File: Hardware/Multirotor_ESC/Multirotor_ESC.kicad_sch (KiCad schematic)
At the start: 0 parts

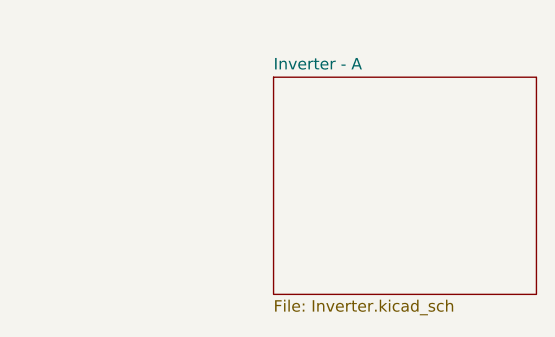
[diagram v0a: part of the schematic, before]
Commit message: Added Phase Half-Bridge Circuit
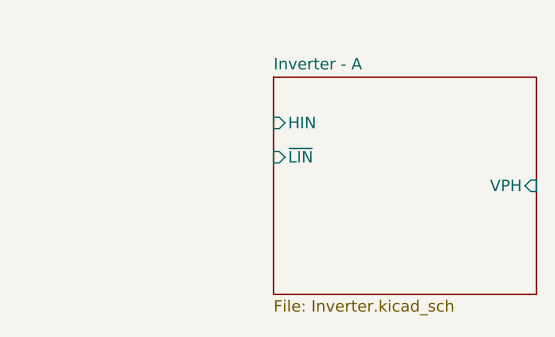
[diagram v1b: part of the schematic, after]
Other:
- sheet Inverter - A ports: added HIN, VPH, ~{LIN}; removed none
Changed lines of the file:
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@@
       (effects (font (size 1.27 1.27)) (justify left top))
+    )
+    (pin "HIN" input (at 135.89 74.93 180)
+      (effects (font (size 1.27 1.27)) (justify left))
+    )
+    (pin "~{LIN}" input (at 135.89 78.74 180)
+      (effects (font (size 1.27 1.27)) (justify left))
+    )
+    (pin "VPH" input (at 165.1 81.915 0)
+      (effects (font (size 1.27 1.27)) (justify right))
     )
   )
@@
       (reference "#PWR?") (unit 1) (value "+BATT") (footprint "")
     )
+    (path "/97e0d8f2-3fb5-4132-bc5b-5e7a03ef2bdb/1fb1d06b-db4f-42d1-9251-2385d7bb41cf"
+      (reference "#PWR?") (unit 1) (value "GND") (footprint "")
+    )
+    (path "/97e0d8f2-3fb5-4132-bc5b-5e7a03ef2bdb/268e3d62-216c-4de0-ba8e-c1e5772f9b92"
+      (reference "#PWR?") (unit 1) (value "+BATT") (footprint "")
+    )
+    (path "/97e0d8f2-3fb5-4132-bc5b-5e7a03ef2bdb/3ca54db6-939c-4fbf-b276-1cff5ae9ba60"
+      (reference "#PWR?") (unit 1) (value "GND") (footprint "")
+    )
+    (path "/97e0d8f2-3fb5-4132-bc5b-5e7a03ef2bdb/574bb345-e256-4887-850f-b8dd578552c6"
+      (reference "#PWR?") (unit 1) (value "GND") (footprint "")
+    )
     (path "/6925d0aa-6a6d-48e8-beb5-c68f11da7a23/727fd17b-2514-45b6-a580-bec774717ec9"
       (reference "#PWR?") (unit 1) (value "GND") (footprint "")
@@
       (reference "#PWR?") (unit 1) (value "+3V3") (footprint "")
     )
+    (path "/97e0d8f2-3fb5-4132-bc5b-5e7a03ef2bdb/85d6321a-5bef-4003-9692-bf4bf59b33cc"
+      (reference "#PWR?") (unit 1) (value "GND") (footprint "")
+    )
+    (path "/97e0d8f2-3fb5-4132-bc5b-5e7a03ef2bdb/9fbafe7a-b33b-4a4e-b582-f71e3fabfd8e"
+      (reference "#PWR?") (unit 1) (value "+3V3") (footprint "")
+    )
+    (path "/97e0d8f2-3fb5-4132-bc5b-5e7a03ef2bdb/a8699dfc-87f8-4653-a4c7-dfff237c52ef"
+      (reference "#PWR?") (unit 1) (value "GND") (footprint "")
+    )
+    (path "/97e0d8f2-3fb5-4132-bc5b-5e7a03ef2bdb/f2234975-42e9-48d9-8b53-ca208cf03c75"
+      (reference "#PWR?") (unit 1) (value "+BATT") (footprint "")
+    )
+    (path "/97e0d8f2-3fb5-4132-bc5b-5e7a03ef2bdb/089f6096-ba98-4aaa-8bdf-ede1c7ae272e"
+      (reference "C?") (unit 1) (value "47μF") (footprint "")
+    )
     (path "/6925d0aa-6a6d-48e8-beb5-c68f11da7a23/666b110b-64b3-4b1b-b648-8cefb6eb0bcb"
       (reference "C?") (unit 1) (value "100nF") (footprint "")
@@
     )
     (path "/6925d0aa-6a6d-48e8-beb5-c68f11da7a23/7d444e59-e85f-4b36-a7ee-89b1c2dc2bc1"
-      (reference "C?") (unit 1) (value "47uF") (footprint "")
+      (reference "C?") (unit 1) (value "47μF") (footprint "")
     )
     (path "/6925d0aa-6a6d-48e8-beb5-c68f11da7a23/7f018784-9df3-41a8-a771-7183d616fcb0"
       (reference "C?") (unit 1) (value "100nF") (footprint "")
+    )
+    (path "/97e0d8f2-3fb5-4132-bc5b-5e7a03ef2bdb/bd46a2b4-b92a-4936-9d7c-11eee0e384a6"
+      (reference "C?") (unit 1) (value "1μF") (footprint "")
+    )
+    (path "/97e0d8f2-3fb5-4132-bc5b-5e7a03ef2bdb/bd887885-43f0-4985-a387-d5bffe1a774c"
+      (reference "C?") (unit 1) (value "1μF") (footprint "")
+    )
+    (path "/97e0d8f2-3fb5-4132-bc5b-5e7a03ef2bdb/c9a91d26-ba86-4e5a-a536-67083e503fde"
+      (reference "C?") (unit 1) (value "1nF") (footprint "")
+    )
+    (path "/97e0d8f2-3fb5-4132-bc5b-5e7a03ef2bdb/cd75599b-50b9-4b16-8dec-26d684651b26"
+      (reference "C?") (unit 1) (value "100nF") (footprint "")
+    )
+    (path "/97e0d8f2-3fb5-4132-bc5b-5e7a03ef2bdb/d7576022-7064-48aa-bc88-f7217e8093a0"
+      (reference "C?") (unit 1) (value "10nF") (footprint "")
     )
     (path "/6925d0aa-6a6d-48e8-beb5-c68f11da7a23/e44df006-a55a-47e0-86b1-17debb1f8182"
@@
       (reference "D?") (unit 1) (value "LED") (footprint "")
     )
+    (path "/97e0d8f2-3fb5-4132-bc5b-5e7a03ef2bdb/2902243c-a616-4e0b-b976-e66ba39b0725"
+      (reference "D?") (unit 1) (value "D_TVS") (footprint "")
+    )
+    (path "/97e0d8f2-3fb5-4132-bc5b-5e7a03ef2bdb/ae845764-3102-4eea-9c30-798c6cae01d9"
+      (reference "D?") (unit 1) (value "D_Schottky") (footprint "")
+    )
     (path "/6925d0aa-6a6d-48e8-beb5-c68f11da7a23/af026ffe-ca2f-412b-8e63-3ecf96ad32af"
       (reference "D?") (unit 1) (value "D_TVS") (footprint "")
@@
       (reference "L?") (unit 1) (value "120R") (footprint "")
     )
+    (path "/97e0d8f2-3fb5-4132-bc5b-5e7a03ef2bdb/48372f14-952c-4ead-9841-6a6b01cb6ba9"
+      (reference "Q?") (unit 1) (value "SIR182DP-T1-RE3") (footprint "")
+    )
+    (path "/97e0d8f2-3fb5-4132-bc5b-5e7a03ef2bdb/9247a4d0-19a2-4ebd-8ef1-fdbc5bc16073"
+      (reference "Q?") (unit 1) (value "SIR182DP-T1-RE3") (footprint "")
+    )
+    (path "/97e0d8f2-3fb5-4132-bc5b-5e7a03ef2bdb/13ac03c9-514f-4610-a1ef-8c14da688496"
+      (reference "R?") (unit 1) (value "4.7kΩ") (footprint "")
+    )
     (path "/6925d0aa-6a6d-48e8-beb5-c68f11da7a23/248ead7f-752e-40c0-bb8c-4be19db10e0d"
       (reference "R?") (unit 1) (value "75kΩ") (footprint "")
+    )
+    (path "/97e0d8f2-3fb5-4132-bc5b-5e7a03ef2bdb/2623340c-6824-413a-b561-66c38b004f8f"
+      (reference "R?") (unit 1) (value "100Ω") (footprint "")
     )
     (path "/6925d0aa-6a6d-48e8-beb5-c68f11da7a23/30884663-b4d1-4804-b0f3-0861de72726b"
@@
       (reference "R?") (unit 1) (value "110kΩ") (footprint "")
     )
+    (path "/97e0d8f2-3fb5-4132-bc5b-5e7a03ef2bdb/5b0936e7-7161-47fa-9186-e44375fa52b6"
+      (reference "R?") (unit 1) (value "100Ω") (footprint "")
+    )
+    (path "/97e0d8f2-3fb5-4132-bc5b-5e7a03ef2bdb/5e26f97d-fab6-49a2-a541-bc2264f9522b"
+      (reference "R?") (unit 1) (value "2mΩ") (footprint "")
+    )
     (path "/6925d0aa-6a6d-48e8-beb5-c68f11da7a23/690f7831-bbd0-434d-9bf7-2f33f2b678b2"
       (reference "R?") (unit 1) (value "12kΩ") (footprint "")
@@
       (reference "R?") (unit 1) (value "1kΩ") (footprint "")
     )
+    (path "/97e0d8f2-3fb5-4132-bc5b-5e7a03ef2bdb/aca084b7-8df0-4d93-9d6c-b5b0ceddd281"
+      (reference "R?") (unit 1) (value "1kΩ") (footprint "")
+    )
     (path "/6925d0aa-6a6d-48e8-beb5-c68f11da7a23/dbf9d707-36a7-44c9-8154-2c0ba309d498"
       (reference "R?") (unit 1) (value "24kΩ") (footprint "")
+    )
+    (path "/97e0d8f2-3fb5-4132-bc5b-5e7a03ef2bdb/e00eda02-ebfb-4c4b-9080-81449d9715cf"
+      (reference "R?") (unit 1) (value "1kΩ") (footprint "")
     )
     (path "/6925d0aa-6a6d-48e8-beb5-c68f11da7a23/fe9632fd-6344-4254-bb7c-69d57a7190da"
       (reference "R?") (unit 1) (value "4.7kΩ") (footprint "")
     )
+    (path "/97e0d8f2-3fb5-4132-bc5b-5e7a03ef2bdb/6d254fa2-e95b-4d81-85ec-158eceec45b3"
+      (reference "U?") (unit 1) (value "INA180") (footprint "Package_TO_SOT_SMD:SOT-23-5")
+    )
     (path "/6925d0aa-6a6d-48e8-beb5-c68f11da7a23/c13cf85f-c98f-45ba-8820-17fab98a6470"

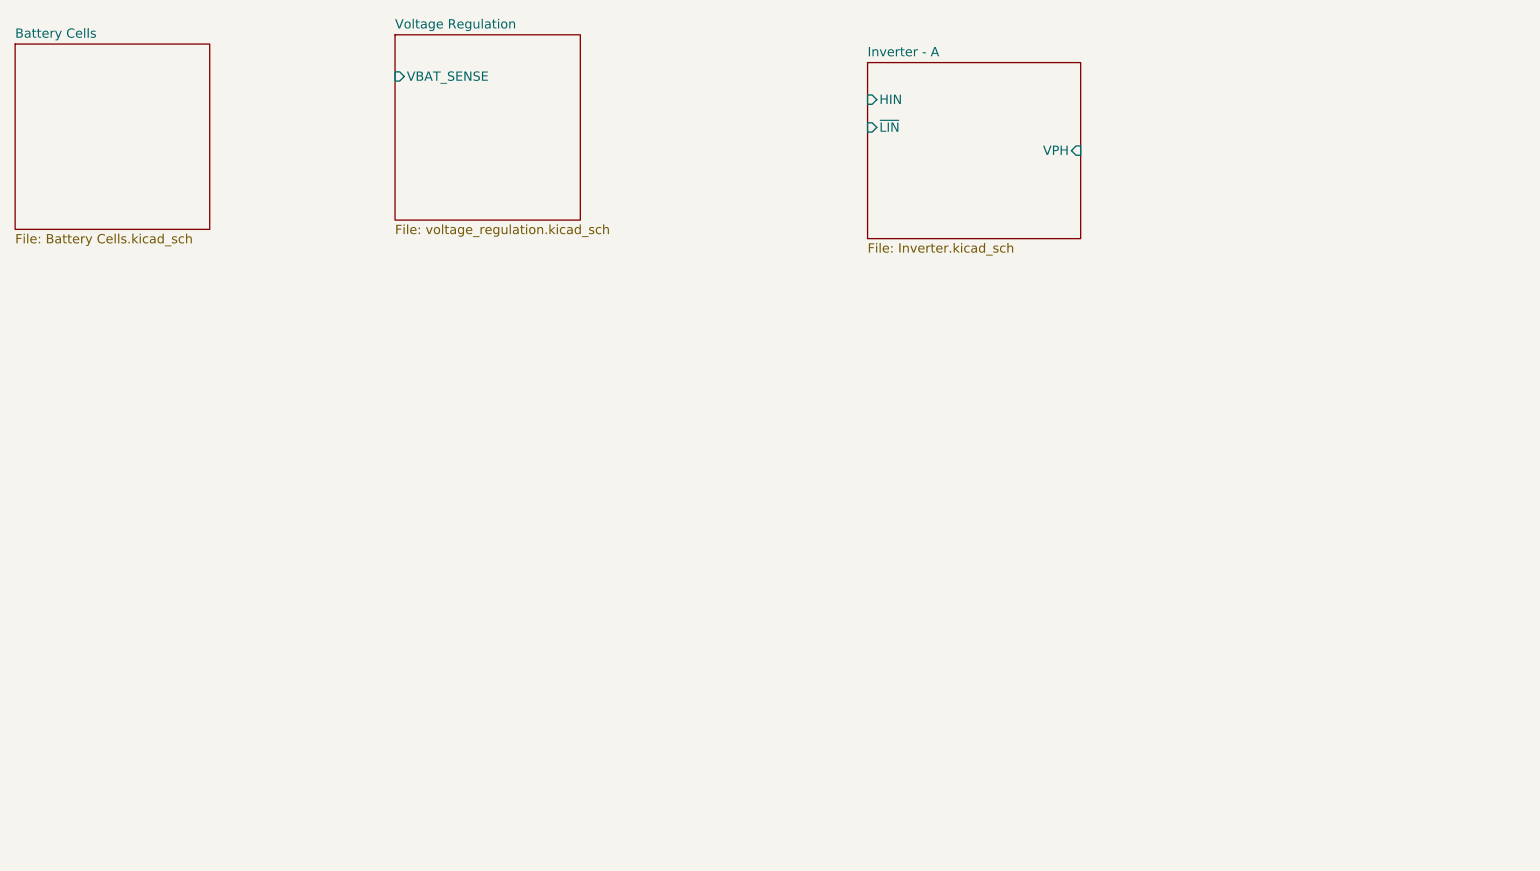
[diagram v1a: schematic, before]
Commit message: Added motor connector and microcontroller sheet
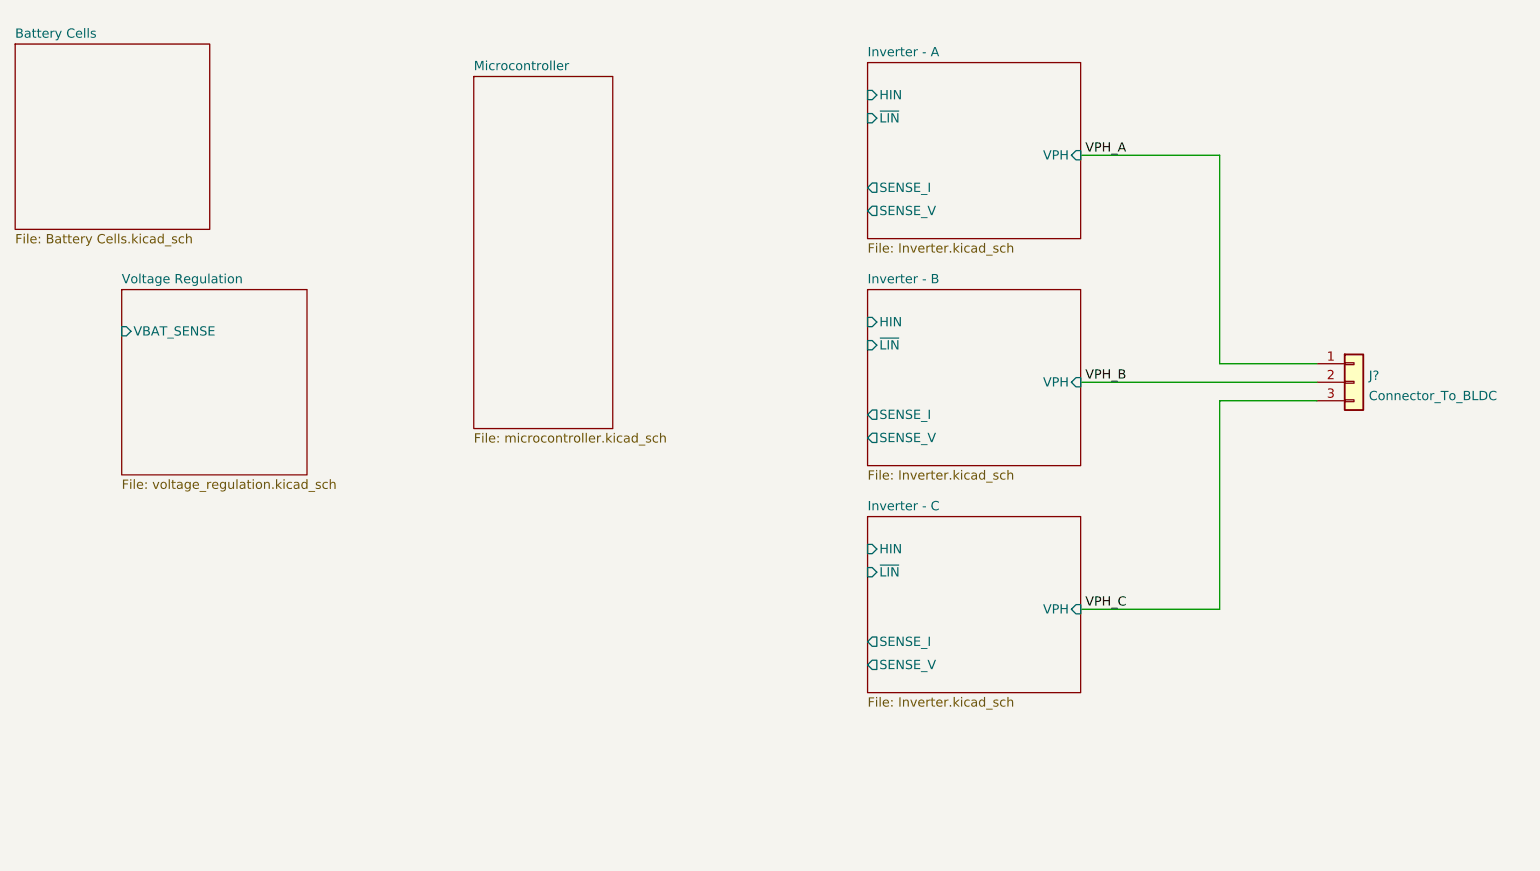
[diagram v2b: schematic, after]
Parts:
- added J?: Connector_To_BLDC, symbol Connector_Generic:Conn_01x03
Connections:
- new net VPH_A: J?.1 (Pin_1)
- new net VPH_B: J?.2 (Pin_2)
- new net VPH_C: J?.3 (Pin_3)
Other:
- added sheet Inverter - B (Inverter.kicad_sch)
- added sheet Inverter - C (Inverter.kicad_sch)
- added sheet Microcontroller (microcontroller.kicad_sch)
- sheet Inverter - A ports: added SENSE_I, SENSE_V; removed none

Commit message: Reorganized sheets
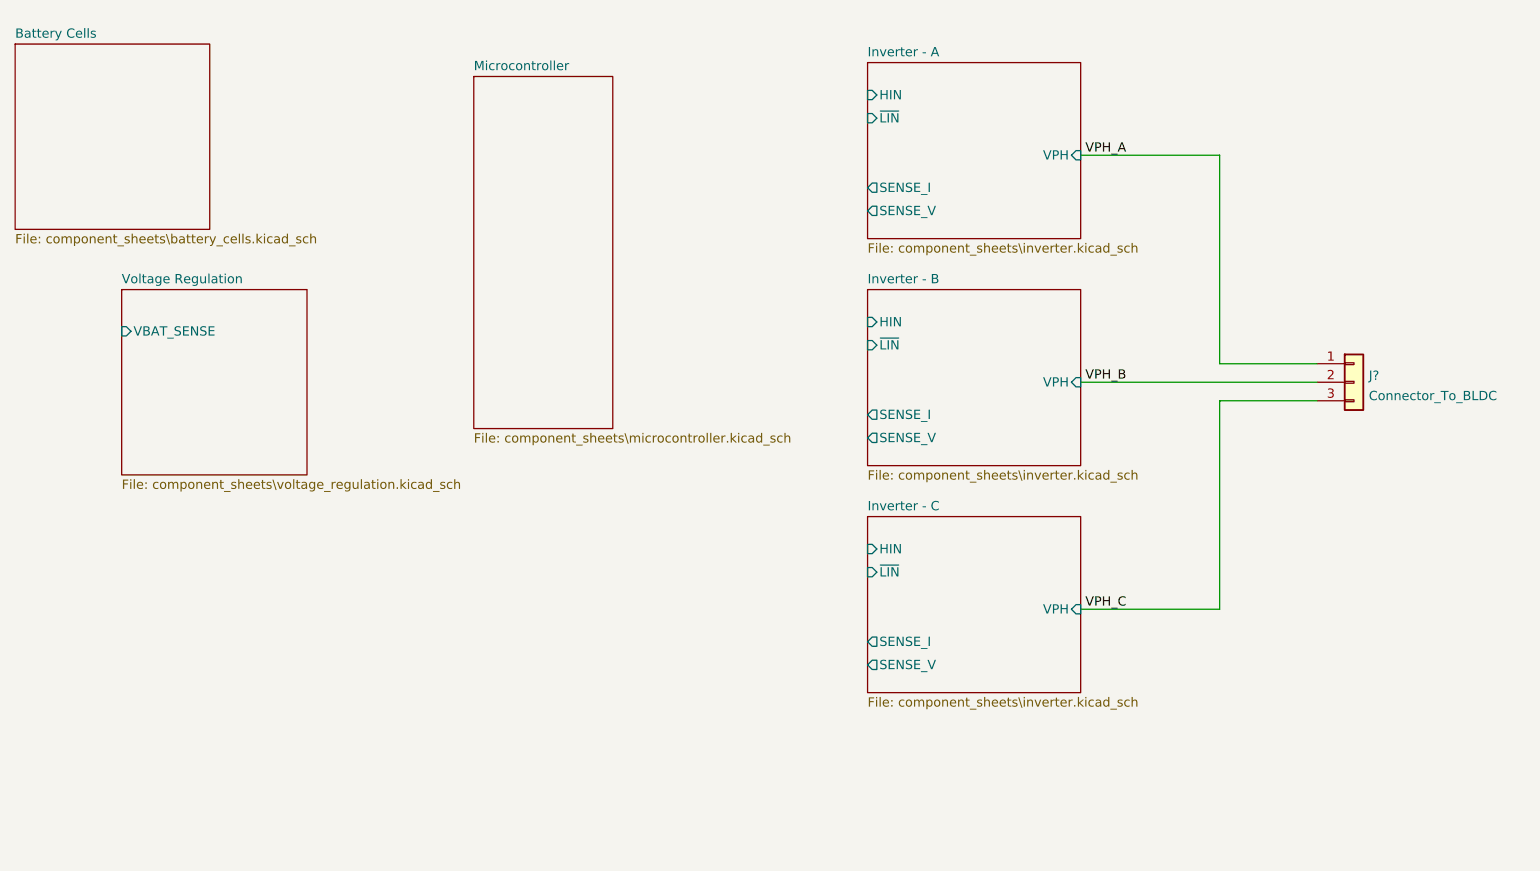
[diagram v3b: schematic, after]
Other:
- sheet Battery Cells: file Battery Cells.kicad_sch -> component_sheets\battery_cells.kicad_sch
- sheet Inverter - A: file Inverter.kicad_sch -> component_sheets\inverter.kicad_sch
- sheet Inverter - B: file Inverter.kicad_sch -> component_sheets\inverter.kicad_sch
- sheet Inverter - C: file Inverter.kicad_sch -> component_sheets\inverter.kicad_sch
- sheet Microcontroller: file microcontroller.kicad_sch -> component_sheets\microcontroller.kicad_sch
- sheet Voltage Regulation: file voltage_regulation.kicad_sch -> component_sheets\voltage_regulation.kicad_sch

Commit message: Improve signage and sheet descriptions
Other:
- title: Multirotor ESC Board -> Multirotor ESC Board - System Overview
